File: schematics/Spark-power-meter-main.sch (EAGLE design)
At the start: 22 parts, among them J1 22-23-2021, J2 22-23-2021, Q1 2N2222A

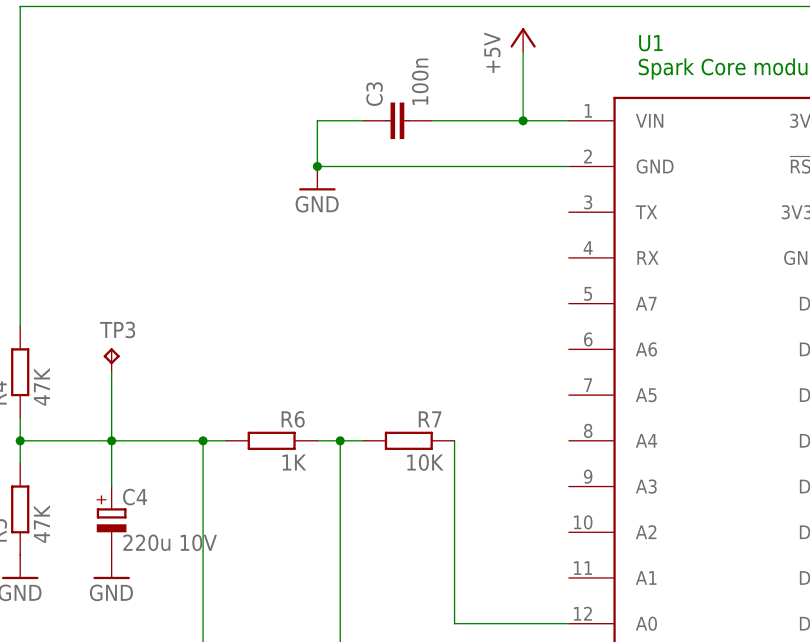
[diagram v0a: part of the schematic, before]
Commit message: power-monitor: save updated schematic
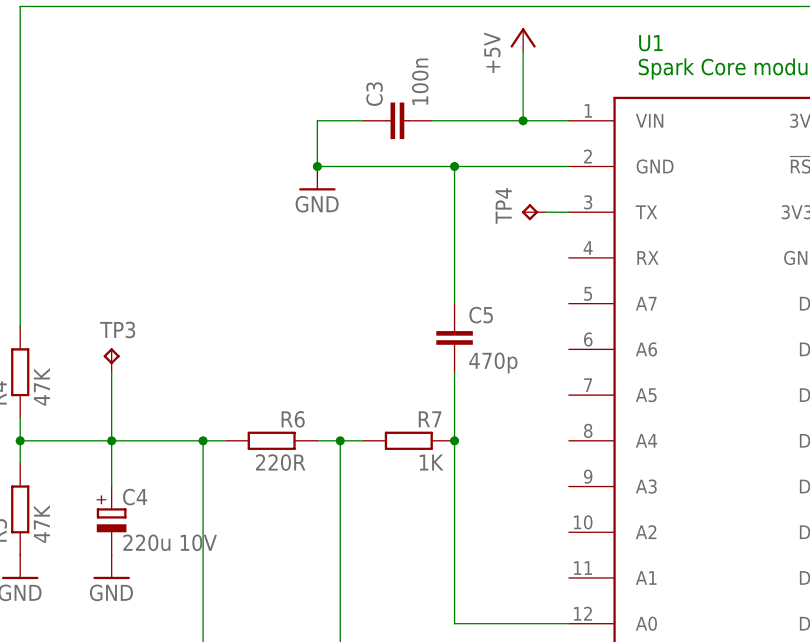
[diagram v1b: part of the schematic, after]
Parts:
- added C5: 470p, rcl:C-EU075-032X103
- added TP4: TPB1,27, testpad:TPB1,27
- R6: value 1K -> 220R
- R7: value 10K -> 1K
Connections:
- new net N$8: TP4.TP, U$1.TX
- net GND: now also C5.1
- net N$9: now also C5.2
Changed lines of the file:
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@@
 <part name="R4" library="resistor" deviceset="R-EU_" device="0207/10" value="47K"/>
 <part name="R5" library="resistor" deviceset="R-EU_" device="0207/10" value="47K"/>
-<part name="R6" library="resistor" deviceset="R-EU_" device="0207/10" value="1K"/>
-<part name="R7" library="resistor" deviceset="R-EU_" device="0207/10" value="10K"/>
+<part name="R6" library="resistor" deviceset="R-EU_" device="0207/10" value="220R"/>
+<part name="R7" library="resistor" deviceset="R-EU_" device="0207/10" value="1K"/>
 <part name="GND5" library="supply1" deviceset="GND" device=""/>
 <part name="GND6" library="supply1" deviceset="GND" device=""/>
@@
 <part name="TP2" library="testpad" deviceset="TP" device="B1,27"/>
 <part name="TP3" library="testpad" deviceset="TP" device="B1,27"/>
+<part name="TP4" library="testpad" deviceset="TP" device="B1,27"/>
+<part name="C5" library="rcl" deviceset="C-EU" device="075-032X103" value="470p"/>
 </parts>
 <sheets>
@@
 <instance part="TP2" gate="G$1" x="127" y="106.68"/>
 <instance part="TP3" gate="G$1" x="7.62" y="-7.62"/>
+<instance part="TP4" gate="G$1" x="53.34" y="7.62" rot="R90"/>
+<instance part="C5" gate="G$1" x="45.72" y="-5.08"/>
 </instances>
 <busses>
@@
 <wire x1="35.56" y1="17.78" x2="30.48" y2="17.78" width="0.1524" layer="91"/>
 <pinref part="U$1" gate="G$1" pin="GND@2"/>
-<wire x1="58.42" y1="12.7" x2="30.48" y2="12.7" width="0.1524" layer="91"/>
+<wire x1="58.42" y1="12.7" x2="45.72" y2="12.7" width="0.1524" layer="91"/>
 <pinref part="GND4" gate="1" pin="GND"/>
+<wire x1="45.72" y1="12.7" x2="30.48" y2="12.7" width="0.1524" layer="91"/>
 <wire x1="30.48" y1="17.78" x2="30.48" y2="12.7" width="0.1524" layer="91"/>
 <junction x="30.48" y="12.7"/>
+<pinref part="C5" gate="G$1" pin="1"/>
+<wire x1="45.72" y1="-2.54" x2="45.72" y2="12.7" width="0.1524" layer="91"/>
+<junction x="45.72" y="12.7"/>
 </segment>
 <segment>
@@
 <pinref part="U$1" gate="G$1" pin="A0"/>
 <wire x1="45.72" y1="-38.1" x2="58.42" y2="-38.1" width="0.1524" layer="91"/>
+<pinref part="C5" gate="G$1" pin="2"/>
+<wire x1="45.72" y1="-10.16" x2="45.72" y2="-17.78" width="0.1524" layer="91"/>
+<junction x="45.72" y="-17.78"/>
 </segment>
 </net>
@@
 </segment>
 </net>
+<net name="N$8" class="0">
+<segment>
+<pinref part="TP4" gate="G$1" pin="TP"/>
+<pinref part="U$1" gate="G$1" pin="TX"/>
+<wire x1="55.88" y1="7.62" x2="58.42" y2="7.62" width="0.1524" layer="91"/>
+</segment>
+</net>
